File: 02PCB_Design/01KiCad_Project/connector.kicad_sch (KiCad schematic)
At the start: 7 parts, among them J5 DE9_Receptacle_MountingHoles, J6 MTSW-104-22-L-D-265-RA, J7 Conn_01x06_Pin, U12 MCP2562FD

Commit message: Changed Some Capacitor Sizes, Added Capacitors in Power Gen
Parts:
- renumbered C70 to C76, C71 to C77
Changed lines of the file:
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@@
   (symbol (lib_id "Device:C") (at 120.65 55.88 0) (unit 1)
     (in_bom yes) (on_board yes) (dnp no)
-    (property "Reference" "C71" (at 123.19 54.61 0)
+    (property "Reference" "C77" (at 123.19 54.61 0)
       (effects (font (size 1.27 1.27)) (justify left))
     )
@@
       (project "Testplatine"
         (path "/de27a806-41f8-462d-8678-2476d523bbd9/a9fc49c7-f356-4c2b-bdd5-d12f8bcc20f7/71441778-19c6-49de-8dce-f1083f9dacbc"
-          (reference "C71") (unit 1)
+          (reference "C77") (unit 1)
         )
       )
@@
   (symbol (lib_id "Device:C") (at 102.87 55.88 180) (unit 1)
     (in_bom yes) (on_board yes) (dnp no)
-    (property "Reference" "C70" (at 100.33 57.15 0)
+    (property "Reference" "C76" (at 100.33 57.15 0)
       (effects (font (size 1.27 1.27)) (justify left))
     )
@@
       (project "Testplatine"
         (path "/de27a806-41f8-462d-8678-2476d523bbd9/a9fc49c7-f356-4c2b-bdd5-d12f8bcc20f7/71441778-19c6-49de-8dce-f1083f9dacbc"
-          (reference "C70") (unit 1)
+          (reference "C76") (unit 1)
         )
       )

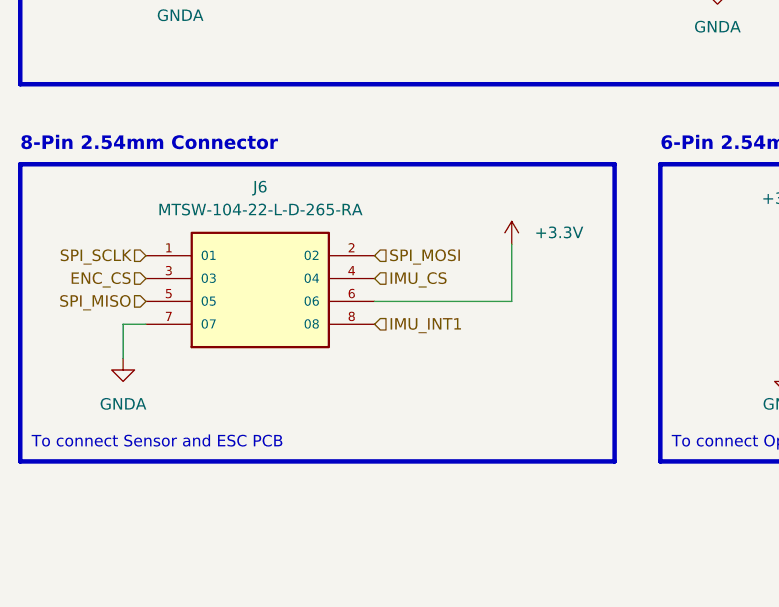
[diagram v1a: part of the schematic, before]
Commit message: All Signals Connected, Ethernet Cable
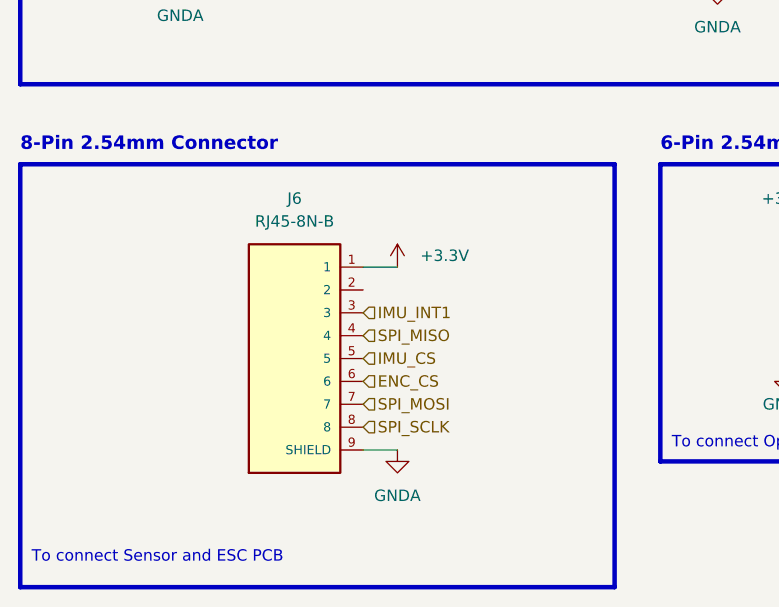
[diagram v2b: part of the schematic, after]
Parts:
- removed J6: MTSW-104-22-L-D-265-RA, Connector_PinHeader_2.54mm:PinHeader_2x04_P2.54mm_Horizontal, symbol MTSW-104-22-L-D-265-RA:MTSW-104-22-L-D-265-RA
- added J6: RJ45-8N-B, RJ45-8N-B:TE_RJ45-8N-B, symbol RJ45-8N-B:RJ45-8N-B
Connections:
- net +3.3V: now also J6.1
- net ENC_CS: now also J6.6
- net GNDA: now also J6.10 (SHIELD), J6.9 (SHIELD)
- net IMU_CS: now also J6.5
- net IMU_INT1: now also J6.3
- net SPI_MISO: now also J6.4
- net SPI_MOSI: now also J6.7
- net SPI_SCLK: now also J6.8

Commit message: edited footprints
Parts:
- removed J6: RJ45-8N-B, RJ45-8N-B:TE_RJ45-8N-B, symbol RJ45-8N-B:RJ45-8N-B
- added J7: RJ45-8N-B, MyFootprintLib:Wurth_634008_RJ45, symbol RJ45-8N-B:RJ45-8N-B
- renumbered J7 to J6
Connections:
- net +3.3V: now also J7.1
- net ENC_CS: now also J7.7
- net GNDA: now also J7.5, J7.SHIELD
- net IMU_CS: now also J7.4
- net IMU_INT1: now also J7.3
- net SPI_MISO: now also J7.8
- net SPI_MOSI: now also J7.2
- net SPI_SCLK: now also J7.6

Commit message: Edited some connectors
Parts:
- J7: value RJ45-8N-B -> Wurth-634008
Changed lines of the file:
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@@
       (effects (font (size 1.27 1.27)))
     )
-    (property "Value" "RJ45-8N-B" (at 110.49 121.92 0)
+    (property "Value" "Wurth-634008" (at 110.49 121.92 0)
       (effects (font (size 1.27 1.27)))
     )

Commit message: relayout in progress
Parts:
- added R47, R48: 0R, Resistor_SMD:R_0603_1608Metric_Pad0.98x0.95mm_HandSolder, symbol Device:R
- C76, C77: value 0.1uF -> 100nF
- J5: value DE9_Receptacle_MountingHoles -> RS PRO 528 D-Sub 2.77mm
- R42: value 120 -> 120R
- U12: value MCP2562FD -> MCP2562FD-E/MF; footprint Package_SO:SOIC-8_3.9x4.9mm_P1.27mm -> Package_DFN_QFN:DFN-8-1EP_3x3mm_P0.65mm_EP1.55x2.4mm
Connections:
- net GNDA: now also U12.9 (EP)
- net at R42.1, U12.7 (CANH): now also R47.1; no longer J5.7
- net at R42.2, U12.6 (CANL): now also R48.2; no longer J5.2
- new net: J5.2, R48.1
- new net: J5.7, R47.2
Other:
- moved on the sheet: J5
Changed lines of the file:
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@@
   (junction (at 97.79 91.44) (diameter 0) (color 0 0 0 0)
   )
+  (junction (at 111.76 91.44) (diameter 0) (color 0 0 0 0)
+  )
   (junction (at 157.48 93.98) (diameter 0) (color 0 0 0 0)
   )
@@
   (junction (at 138.43 81.28) (diameter 0) (color 0 0 0 0)
   )
-  (no_connect (at 161.29 85.09))
-  (no_connect (at 161.29 77.47))
-  (no_connect (at 161.29 82.55))
-  (no_connect (at 161.29 64.77))
-  (no_connect (at 161.29 80.01))
-  (wire (pts (xy 148.59 69.85) (xy 161.29 69.85))
-    (stroke (width 0) (type default))
-  )
-  (wire (pts (xy 138.43 72.39) (xy 161.29 72.39))
-    (stroke (width 0) (type default))
-  )
+  (no_connect (at 179.07 85.09))
+  (no_connect (at 179.07 77.47))
+  (no_connect (at 179.07 82.55))
+  (no_connect (at 179.07 64.77))
+  (no_connect (at 179.07 80.01))
   (wire (pts (xy 97.79 83.82) (xy 97.79 91.44))
     (stroke (width 0) (type default))
@@
     (stroke (width 0) (type default))
   )
-  (wire (pts (xy 152.4 82.55) (xy 161.29 82.55))
+  (wire (pts (xy 152.4 82.55) (xy 179.07 82.55))
     (stroke (width 0) (type default))
   )
@@
     (stroke (width 0) (type default))
   )
-  (wire (pts (xy 168.91 93.98) (xy 157.48 93.98))
+  (wire (pts (xy 186.69 93.98) (xy 157.48 93.98))
     (stroke (width 0) (type default))
   )
@@
     (stroke (width 0) (type default))
   )
+  (wire (pts (xy 148.59 69.85) (xy 165.1 69.85))
+    (stroke (width 0) (type default))
+  )
   (wire (pts (xy 157.48 67.31) (xy 157.48 74.93))
     (stroke (width 0) (type default))
@@
     (stroke (width 0) (type default))
   )
+  (wire (pts (xy 116.84 91.44) (xy 116.84 90.17))
+    (stroke (width 0) (type default))
+  )
+  (wire (pts (xy 116.84 91.44) (xy 111.76 91.44))
+    (stroke (width 0) (type default))
+  )
   (wire (pts (xy 165.1 123.19) (xy 165.1 130.81))
     (stroke (width 0) (type default))
@@
     (stroke (width 0) (type default))
   )
-  (wire (pts (xy 161.29 74.93) (xy 157.48 74.93))
+  (wire (pts (xy 138.43 72.39) (xy 165.1 72.39))
+    (stroke (width 0) (type default))
+  )
+  (wire (pts (xy 179.07 74.93) (xy 157.48 74.93))
+    (stroke (width 0) (type default))
+  )
+  (wire (pts (xy 172.72 69.85) (xy 179.07 69.85))
     (stroke (width 0) (type default))
   )
@@
     (stroke (width 0) (type default))
   )
-  (wire (pts (xy 161.29 67.31) (xy 157.48 67.31))
-    (stroke (width 0) (type default))
-  )
-  (wire (pts (xy 168.91 90.17) (xy 168.91 93.98))
+  (wire (pts (xy 179.07 67.31) (xy 157.48 67.31))
+    (stroke (width 0) (type default))
+  )
+  (wire (pts (xy 186.69 90.17) (xy 186.69 93.98))
     (stroke (width 0) (type default))
   )
   (wire (pts (xy 138.43 81.28) (xy 138.43 80.01))
+    (stroke (width 0) (type default))
+  )
+  (wire (pts (xy 172.72 72.39) (xy 179.07 72.39))
     (stroke (width 0) (type default))
   )
@@
       (effects (font (size 1.27 1.27)) (justify left))
     )
-    (property "Value" "0.1uF" (at 123.19 57.15 0)
+    (property "Value" "100nF" (at 123.19 57.15 0)
       (effects (font (size 1.27 1.27)) (justify left))
     )
@@
       (effects (font (size 1.27 1.27)) (justify left))
     )
-    (property "Value" "0.1uF" (at 100.33 54.61 0)
+    (property "Value" "100nF" (at 100.33 54.61 0)
       (effects (font (size 1.27 1.27)) (justify left))
     )
@@
       (effects (font (size 1.27 1.27)) (justify left))
     )
-    (property "Value" "120" (at 140.97 77.47 0)
+    (property "Value" "120R" (at 140.97 77.47 0)
       (effects (font (size 1.27 1.27)) (justify left))
     )
@@
     )
   )
-  (symbol (lib_id "Connector:DE9_Receptacle_MountingHoles") (at 168.91 74.93 0) (unit 1)
-    (in_bom yes) (on_board yes) (dnp no) (fields_autoplaced)
-    (property "Reference" "J5" (at 173.99 73.66 0)
-      (effects (font (size 1.27 1.27)) (justify left))
-    )
-    (property "Value" "DE9_Receptacle_MountingHoles" (at 173.99 76.2 0)
-      (effects (font (size 1.27 1.27)) (justify left))
-    )
-    (property "Footprint" "Connector_Dsub:DSUB-9_Female_Horizontal_P2.77x2.84mm_EdgePinOffset4.94mm_Housed_MountingHolesOffset7.48mm" (at 168.91 74.93 0)
-      (effects (font (size 1.27 1.27)) hide)
-    )
-    (property "Datasheet" " ~" (at 168.91 74.93 0)
+  (symbol (lib_id "Connector:DE9_Receptacle_MountingHoles") (at 186.69 74.93 0) (unit 1)
+    (in_bom yes) (on_board yes) (dnp no) (fields_autoplaced)
+    (property "Reference" "J5" (at 191.77 73.66 0)
+      (effects (font (size 1.27 1.27)) (justify left))
+    )
+    (property "Value" "RS PRO 528 D-Sub 2.77mm" (at 191.77 76.2 0)
+      (effects (font (size 1.27 1.27)) (justify left))
+    )
+    (property "Footprint" "Connector_Dsub:DSUB-9_Female_Horizontal_P2.77x2.84mm_EdgePinOffset4.94mm_Housed_MountingHolesOffset7.48mm" (at 186.69 74.93 0)
+      (effects (font (size 1.27 1.27)) hide)
+    )
+    (property "Datasheet" " ~" (at 186.69 74.93 0)
       (effects (font (size 1.27 1.27)) hide)
     )
@@
     )
   )
+  (symbol (lib_id "Device:R") (at 168.91 72.39 90) (unit 1)
+    (in_bom yes) (on_board yes) (dnp no)
+    (property "Reference" "R47" (at 168.91 74.93 90)
+      (effects (font (size 1.27 1.27)))
+    )
+    (property "Value" "0R" (at 168.91 72.39 90)
+      (effects (font (size 1.27 1.27)))
+    )
+    (property "Footprint" "Resistor_SMD:R_0603_1608Metric_Pad0.98x0.95mm_HandSolder" (at 168.91 74.168 90)
+      (effects (font (size 1.27 1.27)) hide)
+    )
+    (property "Datasheet" "~" (at 168.91 72.39 0)
+      (effects (font (size 1.27 1.27)) hide)
+    )
+    (pin "1")
+    (pin "2")
+    (instances
+      (project "Testplatine"
+        (path "/de27a806-41f8-462d-8678-2476d523bbd9/a9fc49c7-f356-4c2b-bdd5-d12f8bcc20f7/71441778-19c6-49de-8dce-f1083f9dacbc"
+          (reference "R47") (unit 1)
+        )
+      )
+    )
+  )
   (symbol (lib_id "power:+3.3V") (at 165.1 123.19 0) (unit 1)
     (in_bom yes) (on_board yes) (dnp no)
@@
   (symbol (lib_id "MyKiCadLib:MCP2562FD") (at 111.76 71.12 0) (unit 1)
     (in_bom yes) (on_board yes) (dnp no)
-    (property "Reference" "U12" (at 115.57 93.98 0)
-      (effects (font (size 1.27 1.27)) (justify left))
-    )
-    (property "Value" "MCP2562FD" (at 120.65 90.17 0)
-      (effects (font (size 1.27 1.27)))
-    )
-    (property "Footprint" "Package_SO:SOIC-8_3.9x4.9mm_P1.27mm" (at 111.76 71.12 0)
+    (property "Reference" "U12" (at 91.44 67.31 0)
+      (effects (font (size 1.27 1.27)) (justify left))
+    )
+    (property "Value" "MCP2562FD-E/MF" (at 96.52 63.5 0)
+      (effects (font (size 1.27 1.27)))
+    )
+    (property "Footprint" "Package_DFN_QFN:DFN-8-1EP_3x3mm_P0.65mm_EP1.55x2.4mm" (at 111.76 71.12 0)
       (effects (font (size 1.27 1.27)) hide)
     )
@@
     (pin "2")
     (pin "1")
+    (pin "9")
     (instances
       (project "Testplatine"
@@
         )
       )
+    )
+  )
+  (symbol (lib_id "Device:R") (at 168.91 69.85 270) (unit 1)
+    (in_bom yes) (on_board yes) (dnp no)
+    (property "Reference" "R48" (at 168.91 67.31 90)
+      (effects (font (size 1.27 1.27)))
+    )
+    (property "Value" "0R" (at 168.91 69.85 90)
+      (effects (font (size 1.27 1.27)))
+    )
+    (property "Footprint" "Resistor_SMD:R_0603_1608Metric_Pad0.98x0.95mm_HandSolder" (at 168.91 68.072 90)
+      (effects (font (size 1.27 1.27)) hide)
+    )
+    (property "Datasheet" "~" (at 168.91 69.85 0)
+      (effects (font (size 1.27 1.27)) hide)
+    )
+    (pin "1")
+    (pin "2")
+    (instances
+      (project "Testplatine"
+        (path "/de27a806-41f8-462d-8678-2476d523bbd9/a9fc49c7-f356-4c2b-bdd5-d12f8bcc20f7/71441778-19c6-49de-8dce-f1083f9dacbc"
+          (reference "R48") (unit 1)
+        )
+      )
